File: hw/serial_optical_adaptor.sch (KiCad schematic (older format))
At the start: 11 parts, among them P1 USB_OTG, U1 LM393

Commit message: A    hw/SMTU2032-1.kicad_mod A    hw/adg3300.dcm A    hw/lp3984.dcm A    hw/lp3984.lib M    hw/serial_optical_adaptor-cache.lib M    hw/serial_optical_adaptor.bak M    hw/serial_optical_adaptor.pro M    hw/serial_optical_adaptor.sch
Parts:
- removed P1: USB_OTG, kicadlib:smd_amphenol_usb_micro-b, symbol USB_OTG
- added C? (x6): C, symbol C
- added IC?: ATMEGA168PA-A, TQFP32, symbol ATMEGA168PA-A
- added P?: CONN_02X03, symbol CONN_02X03
- added P?: CONN_01X01, symbol CONN_01X01
- added P?: CONN_01X04, symbol CONN_01X04
- added P?: Battery, symbol CONN_01X02
- added R?: 100k, symbol R
- added R? (x2): R, symbol R
- added U?: ADG3300, symbol ADG3300
- added U?: LP3984, symbol LP3984
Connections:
- net labels added: AVR_RESET, AVR_RFFE_SCLK, AVR_RFFE_SDATA, ICSP_MISO, ICSP_MOSI, ICSP_SCK, RFFE_SCLK, RFFE_SDATA, Vcc, Vrffe
- net labels removed: SCLK, SDATA, VIO
- wire segments 38 -> 37
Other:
- note removed: "CHECK THIS FITS THE PINOUT\nOF THE WISPRY WS1040 BOARD"
- moved on the sheet: D1, D2, R1, R2, R3, R4, R5, R6, RV1, U1A, U1B

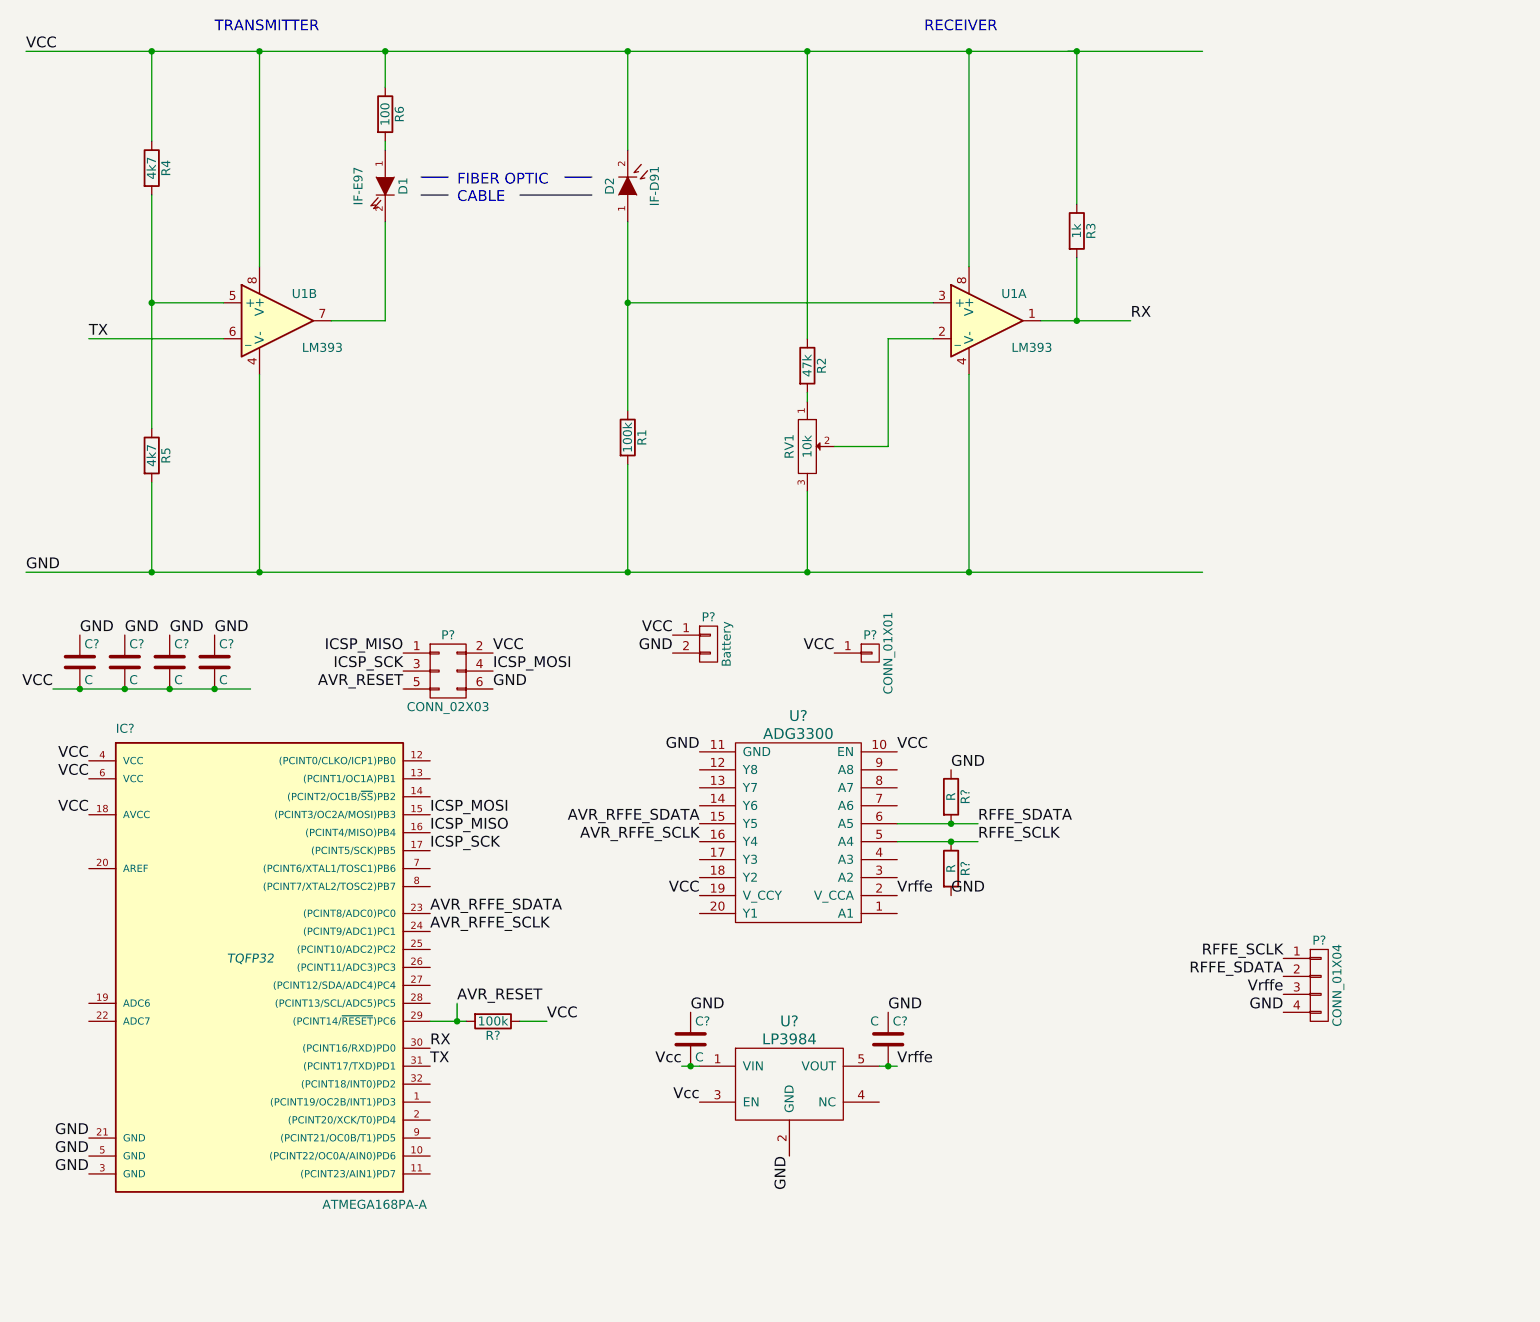
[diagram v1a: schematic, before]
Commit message: 
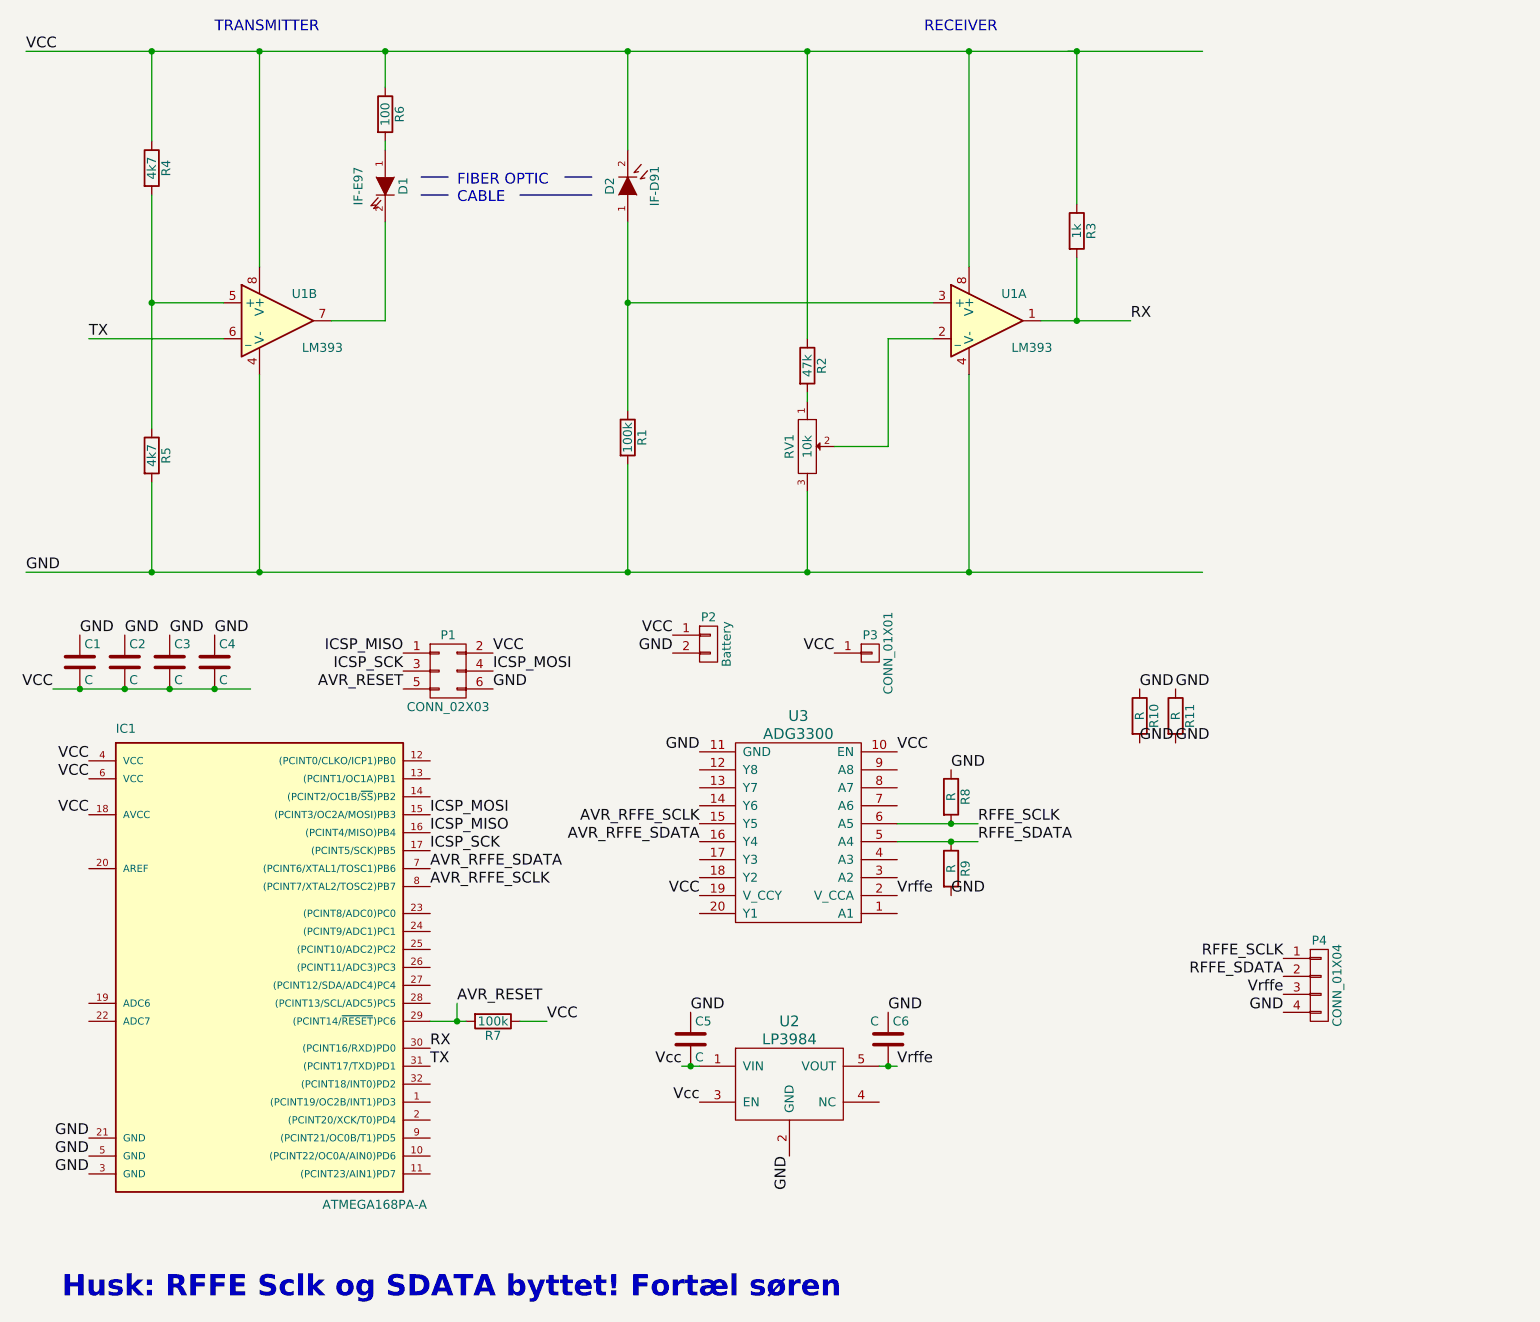
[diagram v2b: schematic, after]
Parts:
- added R10, R11: R, Resistors_SMD:R_0603_HandSoldering, symbol R
- C1, C2, C3, C4, C5, C6: renamed from C?; footprint (none) -> Capacitors_SMD:C_0603_HandSoldering
- IC1: renamed from IC?; footprint TQFP32 -> Housings_QFP:TQFP-32_7x7mm_Pitch0.8mm
- P1: renamed from P?; footprint (none) -> hw:CONN_02X03_SMD
- P2: renamed from P?; footprint (none) -> hw:SMTU2032-1
- P3: renamed from P?; footprint (none) -> hw:CONN_01X01_SMD
- P4: renamed from P?; footprint (none) -> hw:CONN_01X04_SMD
- R7, R8, R9: renamed from R?; footprint (none) -> Resistors_SMD:R_0603_HandSoldering
- RV1: footprint kicadlib:smd_murrata_trimmer_pvz3a -> hw:smd_murrata_trimmer_pvz3a
- U2: renamed from U?; footprint (none) -> TO_SOT_Packages_SMD:SOT-23-5
- U3: renamed from U?; footprint (none) -> hw:TSSOP20
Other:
- note added: "Husk: RFFE Sclk og SDATA byttet! Fortæl søren\n"
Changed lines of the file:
@@
 F 0 "RV1" H 5000 2850 50  0000 C CNN
 F 1 "10k" H 5000 2950 50  0000 C CNN
-F 2 "kicadlib:smd_murrata_trimmer_pvz3a" H 5000 2950 50  0001 C CNN
+F 2 "hw:smd_murrata_trimmer_pvz3a" H 5000 2950 50  0001 C CNN
 F 3 "" H 5000 2950 50  0000 C CNN
 	1    5000 2950
@@
 	2650 1700 2650 2250
 $Comp
-L ATMEGA168PA-A IC?
+L ATMEGA168PA-A IC1
 U 1 1 5704B95B
 P 1900 5800
-F 0 "IC?" H 1150 7050 50  0000 L BNN
+F 0 "IC1" H 1150 7050 50  0000 L BNN
 F 1 "ATMEGA168PA-A" H 2300 4400 50  0000 L BNN
-F 2 "TQFP32" H 1900 5800 50  0000 C CIN
+F 2 "Housings_QFP:TQFP-32_7x7mm_Pitch0.8mm" H 1900 5800 50  0001 C CIN
 F 3 "" H 1900 5800 50  0000 C CNN
 	1    1900 5800
@@
 Text Label 2900 5200 0    60   ~ 0
 ICSP_SCK
-Text Label 2900 5650 0    60   ~ 0
+Text Label 2900 5400 0    60   ~ 0
 AVR_RFFE_SCLK
-Text Label 2900 5550 0    60   ~ 0
+Text Label 2900 5300 0    60   ~ 0
 AVR_RFFE_SDATA
 $Comp
-L ADG3300 U?
+L ADG3300 U3
 U 1 1 5704E7CA
 P 4950 5100
-F 0 "U?" H 4950 4450 60  0000 C CNN
+F 0 "U3" H 4950 4450 60  0000 C CNN
 F 1 "ADG3300" H 4950 4550 60  0000 C CNN
-F 2 "" H 5000 4500 60  0000 C CNN
+F 2 "hw:TSSOP20" H 5000 4500 60  0001 C CNN
 F 3 "" H 5000 4500 60  0000 C CNN
 	1    4950 5100
@@
 Text Label 5500 4650 0    60   ~ 0
 VCC
+Text Label 4400 5150 2    60   ~ 0
+AVR_RFFE_SDATA
 Text Label 4400 5050 2    60   ~ 0
-AVR_RFFE_SDATA
-Text Label 4400 5150 2    60   ~ 0
 AVR_RFFE_SCLK
+Text Label 5950 5150 0    60   ~ 0
+RFFE_SDATA
 Text Label 5950 5050 0    60   ~ 0
-RFFE_SDATA
-Text Label 5950 5150 0    60   ~ 0
 RFFE_SCLK
 $Comp
-L CONN_02X03 P?
+L CONN_02X03 P1
 U 1 1 5704F701
 P 3000 4200
-F 0 "P?" H 3000 4400 50  0000 C CNN
+F 0 "P1" H 3000 4400 50  0000 C CNN
 F 1 "CONN_02X03" H 3000 4000 50  0000 C CNN
-F 2 "" H 3000 3000 50  0000 C CNN
+F 2 "hw:CONN_02X03_SMD" H 3000 3000 50  0001 C CNN
 F 3 "" H 3000 3000 50  0000 C CNN
 	1    3000 4200
@@
 GND
 $Comp
-L LP3984 U?
+L LP3984 U2
 U 1 1 570513A1
 P 4900 6500
-F 0 "U?" H 4900 6850 60  0000 C CNN
+F 0 "U2" H 4900 6850 60  0000 C CNN
 F 1 "LP3984" H 4900 6750 60  0000 C CNN
-F 2 "" H 4600 6050 60  0000 C CNN
+F 2 "TO_SOT_Packages_SMD:SOT-23-5" H 4600 6050 60  0001 C CNN
 F 3 "" H 4600 6050 60  0000 C CNN
 	1    4900 6500
@@
 Vcc
 $Comp
-L C C?
+L C C6
 U 1 1 57051A38
 P 5450 6250
-F 0 "C?" H 5475 6350 50  0000 L CNN
+F 0 "C6" H 5475 6350 50  0000 L CNN
 F 1 "C" H 5350 6350 50  0000 L CNN
-F 2 "" H 5488 6100 50  0000 C CNN
+F 2 "Capacitors_SMD:C_0603_HandSoldering" H 5488 6100 50  0001 C CNN
 F 3 "" H 5450 6250 50  0000 C CNN
 	1    5450 6250
@@
 $EndComp
 $Comp
-L C C?
+L C C5
 U 1 1 57051AAA
 P 4350 6250
-F 0 "C?" H 4375 6350 50  0000 L CNN
+F 0 "C5" H 4375 6350 50  0000 L CNN
 F 1 "C" H 4375 6150 50  0000 L CNN
-F 2 "" H 4388 6100 50  0000 C CNN
+F 2 "Capacitors_SMD:C_0603_HandSoldering" H 4388 6100 50  0001 C CNN
 F 3 "" H 4350 6250 50  0000 C CNN
 	1    4350 6250
@@
 TX
 $Comp
-L R R?
+L R R7
 U 1 1 57052AAB
 P 3250 6150
-F 0 "R?" V 3330 6150 50  0000 C CNN
+F 0 "R7" V 3330 6150 50  0000 C CNN
 F 1 "100k" V 3250 6150 50  0000 C CNN
-F 2 "" V 3180 6150 50  0000 C CNN
+F 2 "Resistors_SMD:R_0603_HandSoldering" V 3180 6150 50  0001 C CNN
 F 3 "" H 3250 6150 50  0000 C CNN
 	1    3250 6150
@@
 AVR_RESET
 $Comp
-L C C?
+L C C1
 U 1 1 5705321A
 P 950 4150
-F 0 "C?" H 975 4250 50  0000 L CNN
+F 0 "C1" H 975 4250 50  0000 L CNN
 F 1 "C" H 975 4050 50  0000 L CNN
-F 2 "" H 988 4000 50  0000 C CNN
+F 2 "Capacitors_SMD:C_0603_HandSoldering" H 988 4000 50  0001 C CNN
 F 3 "" H 950 4150 50  0000 C CNN
 	1    950  4150
@@
 $EndComp
 $Comp
-L C C?
+L C C2
 U 1 1 5705327C
 P 1200 4150
-F 0 "C?" H 1225 4250 50  0000 L CNN
+F 0 "C2" H 1225 4250 50  0000 L CNN
 F 1 "C" H 1225 4050 50  0000 L CNN
-F 2 "" H 1238 4000 50  0000 C CNN
+F 2 "Capacitors_SMD:C_0603_HandSoldering" H 1238 4000 50  0001 C CNN
 F 3 "" H 1200 4150 50  0000 C CNN
 	1    1200 4150
@@
 $EndComp
 $Comp
-L C C?
+L C C3
 U 1 1 570532CD
 P 1450 4150
-F 0 "C?" H 1475 4250 50  0000 L CNN
+F 0 "C3" H 1475 4250 50  0000 L CNN
 F 1 "C" H 1475 4050 50  0000 L CNN
-F 2 "" H 1488 4000 50  0000 C CNN
+F 2 "Capacitors_SMD:C_0603_HandSoldering" H 1488 4000 50  0001 C CNN
 F 3 "" H 1450 4150 50  0000 C CNN
 	1    1450 4150
@@
 $EndComp
 $Comp
-L C C?
+L C C4
 U 1 1 5705332F
 P 1700 4150
-F 0 "C?" H 1725 4250 50  0000 L CNN
+F 0 "C4" H 1725 4250 50  0000 L CNN
 F 1 "C" H 1725 4050 50  0000 L CNN
-F 2 "" H 1738 4000 50  0000 C CNN
+F 2 "Capacitors_SMD:C_0603_HandSoldering" H 1738 4000 50  0001 C CNN
 F 3 "" H 1700 4150 50  0000 C CNN
 	1    1700 4150
@@
 GND
 $Comp
-L CONN_01X01 P?
+L CONN_01X01 P3
 U 1 1 57055043
 P 5350 4100
-F 0 "P?" H 5350 4200 50  0000 C CNN
+F 0 "P3" H 5350 4200 50  0000 C CNN
 F 1 "CONN_01X01" V 5450 4100 50  0000 C CNN
-F 2 "" H 5350 4100 50  0000 C CNN
+F 2 "hw:CONN_01X01_SMD" H 5350 4100 50  0001 C CNN
 F 3 "" H 5350 4100 50  0000 C CNN
 	1    5350 4100
@@
 VCC
 $Comp
-L R R?
+L R R8
 U 1 1 57055B6E
 P 5800 4900
-F 0 "R?" V 5880 4900 50  0000 C CNN
+F 0 "R8" V 5880 4900 50  0000 C CNN
 F 1 "R" V 5800 4900 50  0000 C CNN
-F 2 "" V 5730 4900 50  0000 C CNN
+F 2 "Resistors_SMD:R_0603_HandSoldering" V 5730 4900 50  0001 C CNN
 F 3 "" H 5800 4900 50  0000 C CNN
 	1    5800 4900
@@
 $EndComp
 $Comp
-L R R?
+L R R9
 U 1 1 57055BE0
 P 5800 5300
-F 0 "R?" V 5880 5300 50  0000 C CNN
+F 0 "R9" V 5880 5300 50  0000 C CNN
 F 1 "R" V 5800 5300 50  0000 C CNN
-F 2 "" V 5730 5300 50  0000 C CNN
+F 2 "Resistors_SMD:R_0603_HandSoldering" V 5730 5300 50  0001 C CNN
 F 3 "" H 5800 5300 50  0000 C CNN
 	1    5800 5300
@@
 Connection ~ 6500 750
 $Comp
-L CONN_01X04 P?
+L CONN_01X04 P4
 U 1 1 5705755A
 P 7850 5950
-F 0 "P?" H 7850 6200 50  0000 C CNN
+F 0 "P4" H 7850 6200 50  0000 C CNN
 F 1 "CONN_01X04" V 7950 5950 50  0000 C CNN
-F 2 "" H 7850 5950 50  0000 C CNN
+F 2 "hw:CONN_01X04_SMD" H 7850 5950 50  0001 C CNN
 F 3 "" H 7850 5950 50  0000 C CNN
 	1    7850 5950
@@
 GND
 $Comp
-L CONN_01X02 P?
+L CONN_01X02 P2
 U 1 1 57058EE6
 P 4450 4050
-F 0 "P?" H 4450 4200 50  0000 C CNN
+F 0 "P2" H 4450 4200 50  0000 C CNN
 F 1 "Battery" V 4550 4050 50  0000 C CNN
-F 2 "" H 4450 4050 50  0000 C CNN
+F 2 "hw:SMTU2032-1" H 4450 4050 50  0001 C CNN
 F 3 "" H 4450 4050 50  0000 C CNN
 	1    4450 4050
 	1    0    0    -1
 $EndComp
+$Comp
+L R R10
+U 1 1 57058461
+P 6850 4450
+F 0 "R10" V 6930 4450 50  0000 C CNN
+F 1 "R" V 6850 4450 50  0000 C CNN
+F 2 "Resistors_SMD:R_0603_HandSoldering" V 6780 4450 50  0001 C CNN
+F 3 "" H 6850 4450 50  0000 C CNN
+	1    6850 4450
+	1    0    0    -1
+$EndComp
+$Comp
+L R R11
+U 1 1 570584AE
+P 7050 4450
+F 0 "R11" V 7130 4450 50  0000 C CNN
+F 1 "R" V 7050 4450 50  0000 C CNN
+F 2 "Resistors_SMD:R_0603_HandSoldering" V 6980 4450 50  0001 C CNN
+F 3 "" H 7050 4450 50  0000 C CNN
+	1    7050 4450
+	1    0    0    -1
+$EndComp
+Text Label 6850 4300 0    60   ~ 0
+GND
+Text Label 7050 4300 0    60   ~ 0
+GND
+Text Label 7050 4600 0    60   ~ 0
+GND
+Text Label 6850 4600 0    60   ~ 0
+GND
+Text Notes 850  7700 0    118  ~ 24
+Husk: RFFE Sclk og SDATA byttet! Fortæl søren\n
 $EndSCHEMATC
